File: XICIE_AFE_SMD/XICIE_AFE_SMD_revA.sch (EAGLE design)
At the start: 14 parts, among them IC1 LM324D, Q1 MOSFET-NCHANNELBSS123LT1G, Q2 MOSFET-NCHANNELBSS123LT1G

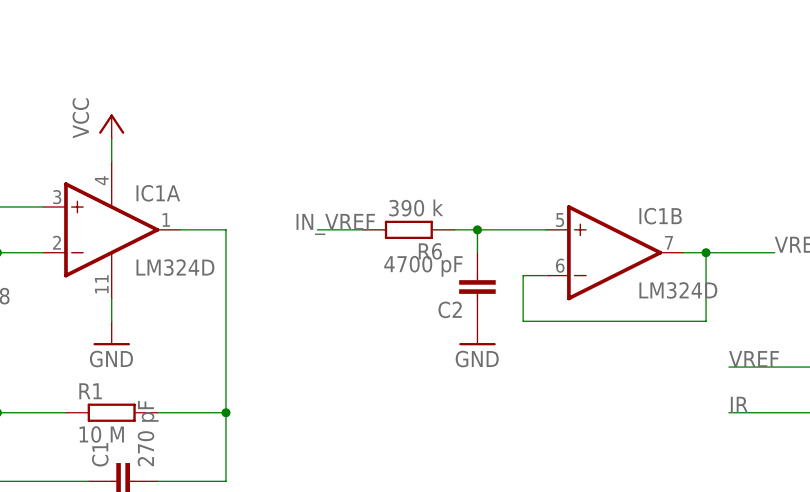
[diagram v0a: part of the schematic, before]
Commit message: Minor changes in afe_smd
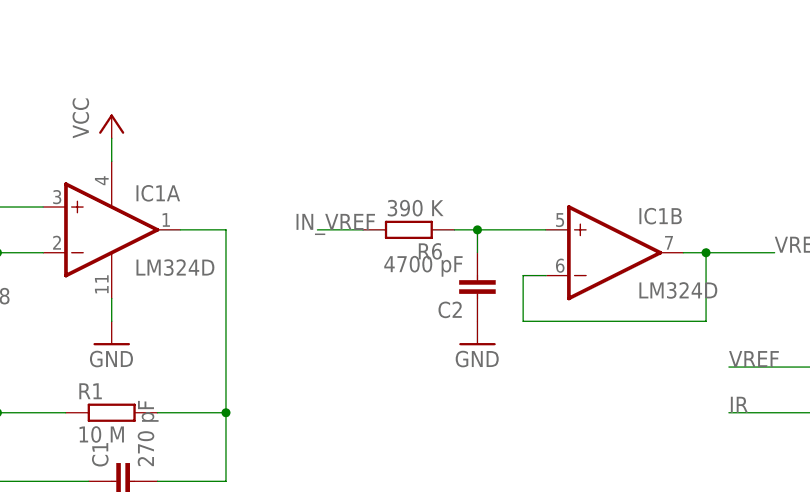
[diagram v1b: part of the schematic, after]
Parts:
- R6: value 390 k -> 390 K
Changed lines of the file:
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@@
 <part name="R4" library="rcl" deviceset="R-EU_" device="R0603" value="10"/>
 <part name="R5" library="rcl" deviceset="R-EU_" device="R0603" value="10"/>
-<part name="R6" library="rcl" deviceset="R-EU_" device="R0603" value="390 k"/>
+<part name="R6" library="rcl" deviceset="R-EU_" device="R0603" value="390 K"/>
 <part name="C2" library="rcl" deviceset="C-EU" device="C0402" value="4700 pF"/>
 <part name="GND4" library="supply1" deviceset="GND" device=""/>

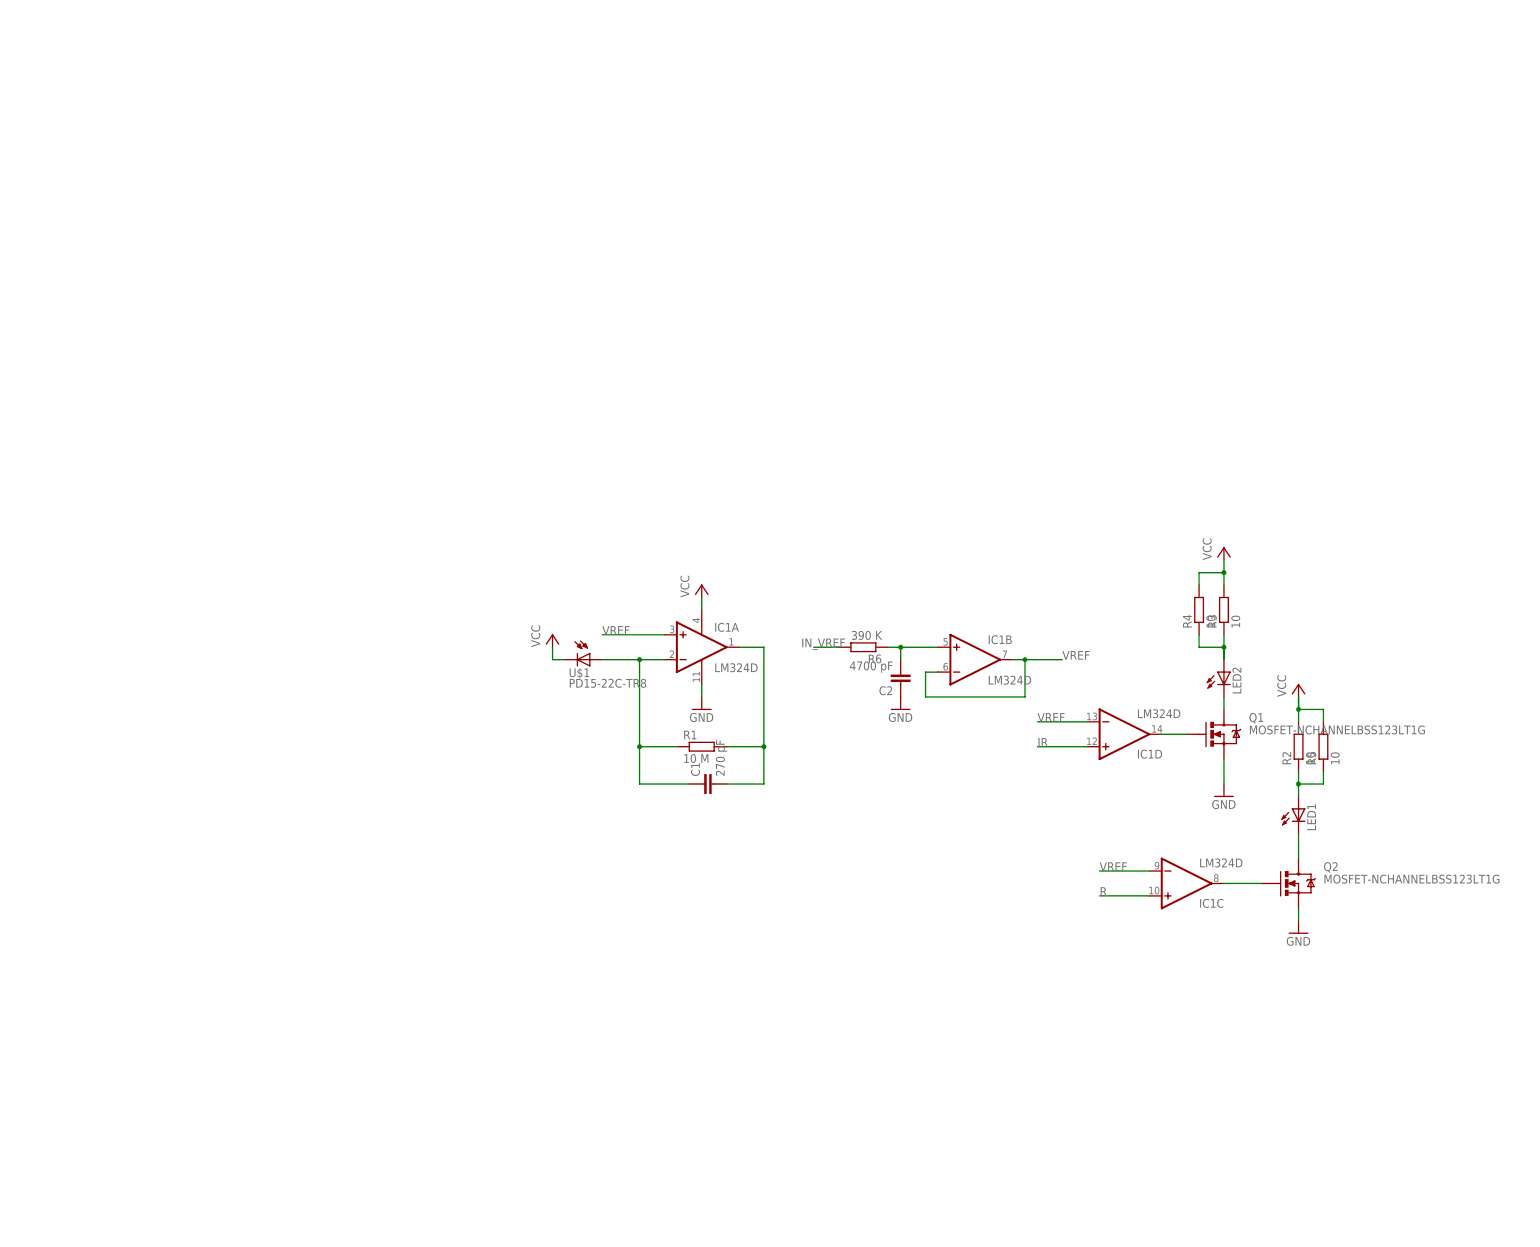
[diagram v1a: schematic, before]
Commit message: Added PSoc IC and boost converter
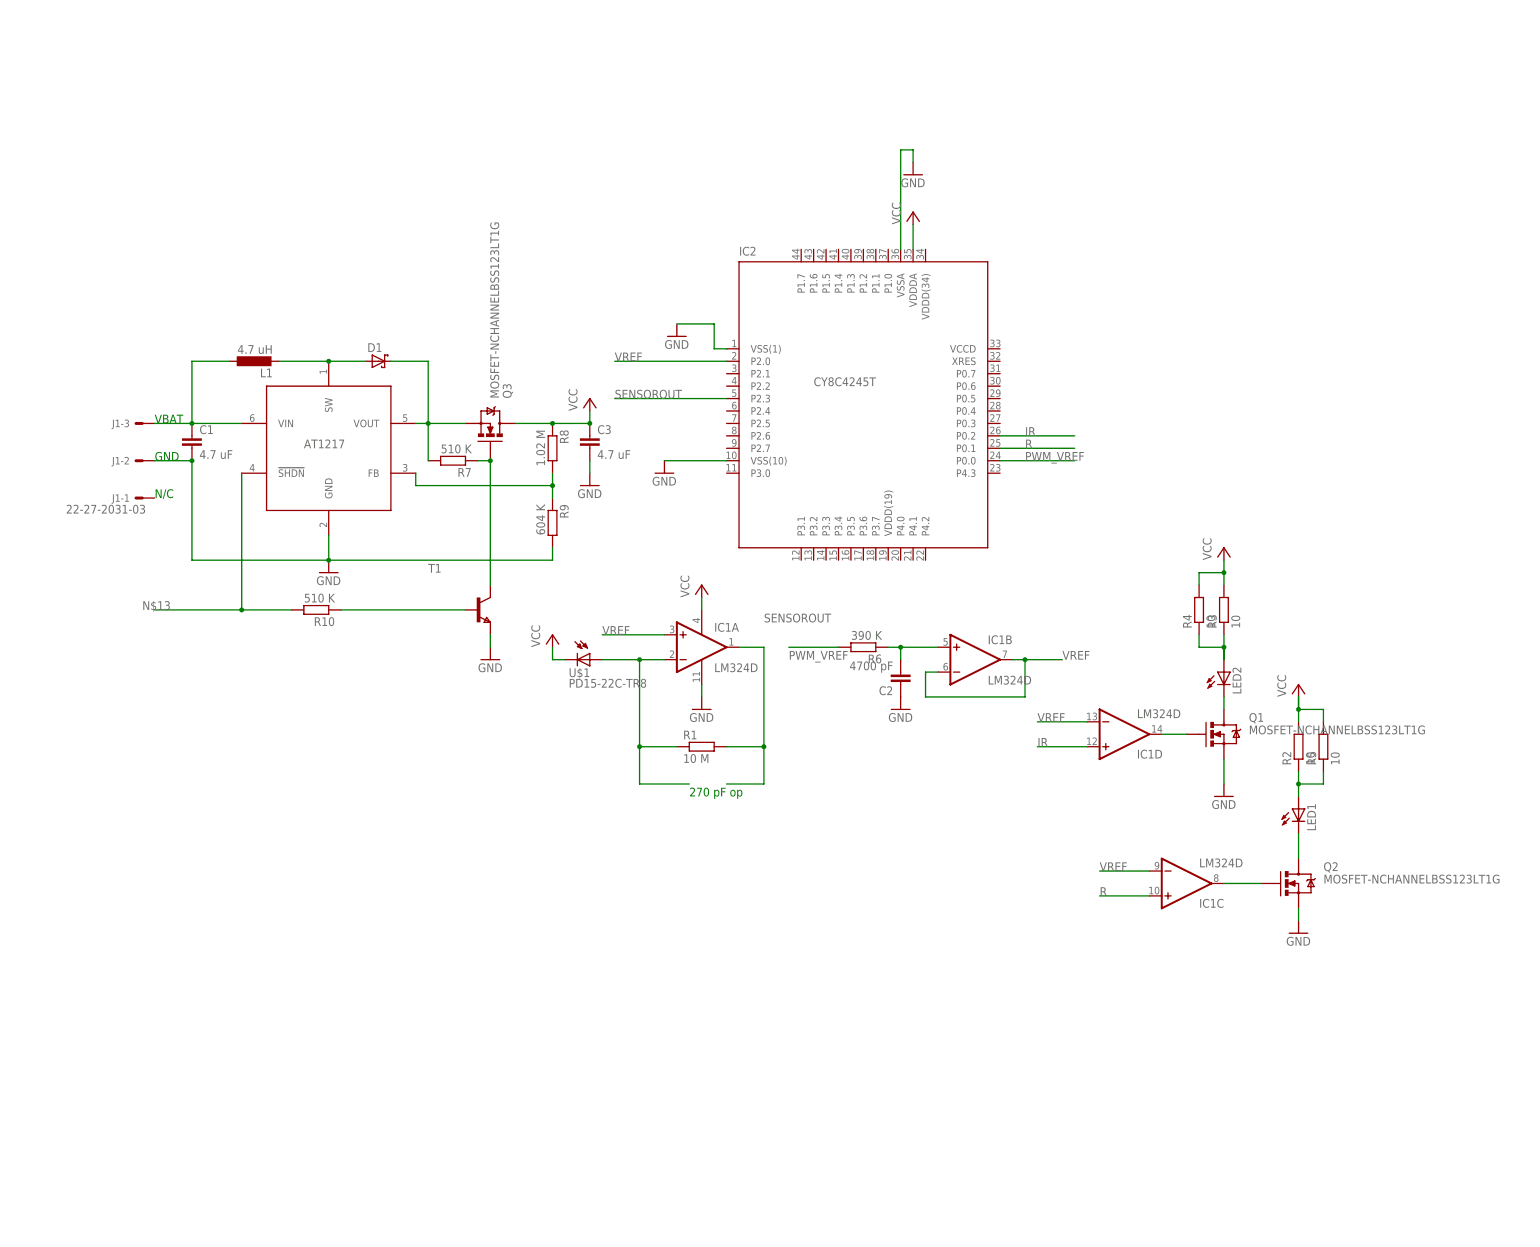
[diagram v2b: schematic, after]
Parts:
- added C3: 4.7 uF, rcl:C-EUC0603
- added D1: (no value), juliano:SCHOTTKY-DIODESMD
- added IC2: CY8C4245T, juliano:CY8C4245T
- added IC3: AAT1217, juliano:AAT1217
- added J1: 22-27-2031-03, con-molex:22-27-2031-03
- added L1: 4.7 uH, juliano:L-EU
- added Q3: MOSFET-NCHANNELBSS123LT1G, SparkFun-DiscreteSemi:MOSFET-NCHANNELBSS123LT1G
- added R10, R7: 510 K, rcl:R-EU_R0603
- added R8: 1.02 M, rcl:R-EU_R0805
- added R9: 604 K, rcl:R-EU_R0603
- added T1: (no value), zetex:NPNSOT23
- C1: value 270 pF -> 4.7 uF; device rcl:C-EUC0402 -> rcl:C-EUC0603
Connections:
- removed net IN_VREF: R6.2
- removed net TRANSOUT: C1.2, IC1A.OUT, R1.2
- new net N$10: C1.1, IC3.VIN, J1-3.S, L1.1
- new net N$11: D1.C, IC3.VOUT, Q3.S, R7.2
- new net N$12: Q3.G, R7.1, T1.C
- new net N$13: IC3.!SHDN, R10.2
- new net N$14: IC3.FB, R8.2, R9.1
- new net N$15: R10.1, T1.B
- new net N$2: D1.A, IC3.SW, L1.2
- new net PWM_VREF: IC2.P0.0, R6.2
- new net SENSOROUT: IC1A.OUT, IC2.P2.3, R1.2
- net GND: now also C1.2, C3.2, IC2.VSS(1), IC2.VSS(10), IC2.VSSA, IC3.GND, J1-2.S, R9.2, T1.E
- net IR: now also IC2.P0.2
- net N$1: no longer C1.1
- net R: now also IC2.P0.1
- net VCC: now also C3.1, IC2.VDDDA, Q3.D, R8.1
- net VREF: now also IC2.P2.0
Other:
- note added: "270 pF op"
- note added: "GND"
- note added: "N/C"
- note added: "VBAT"
- moved on the sheet: C1

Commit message: PCB Layoutd
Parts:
- removed Q3: MOSFET-NCHANNELBSS123LT1G, SparkFun-DiscreteSemi:MOSFET-NCHANNELBSS123LT1G
- removed R10, R7: 510 K, rcl:R-EU_R0603
- removed R5: 10, rcl:R-EU_R0603
- removed T1: (no value), zetex:NPNSOT23
- R2, R3: value 10 -> 1.1; device rcl:R-EU_R0603 -> rcl:R-EU_R0402
- R4: value 10 -> 1.02 M; device rcl:R-EU_R0603 -> rcl:R-EU_R0805
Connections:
- net N$2 renamed SW
- removed net N$10: C1.1, IC3.VIN, J1-3.S, L1.1
- removed net N$11: D1.C, IC3.VOUT, Q3.S, R7.2
- removed net N$12: Q3.G, R7.1, T1.C
- removed net N$13: IC3.!SHDN, R10.2
- removed net N$15: R10.1, T1.B
- new net SHUTDOWN: IC3.!SHDN, R4.2
- new net VBAT: C1.1, IC3.VIN, J1-3.S, L1.1, R4.1
- net GND: no longer T1.E
- net N$7: no longer R5.1
- net N$8: no longer R4.1
- net VCC: now also D1.C, IC3.VOUT; no longer Q3.D, R4.2, R5.2
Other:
- moved on the sheet: R4

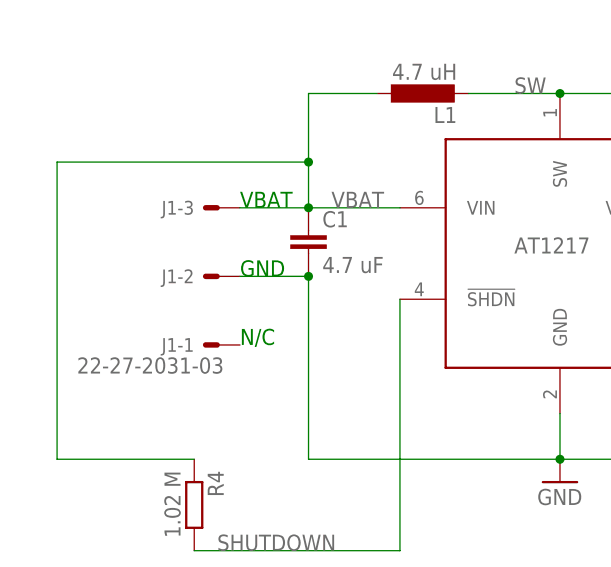
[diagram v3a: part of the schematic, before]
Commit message: Reduced outline
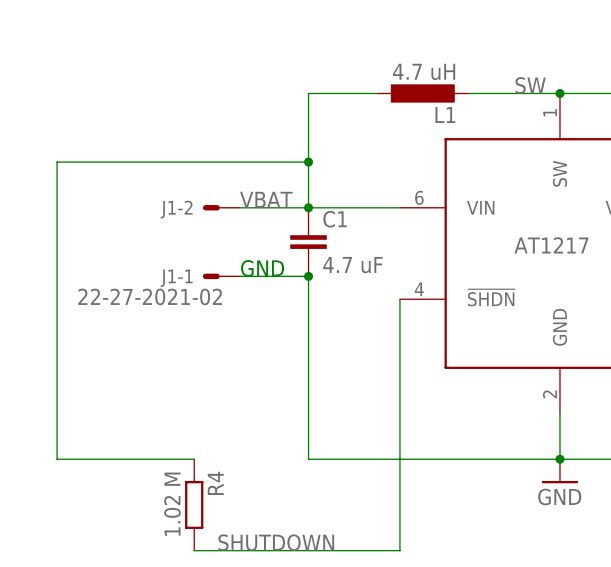
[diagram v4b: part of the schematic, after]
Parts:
- J1: value 22-27-2031-03 -> 22-27-2021-02; device con-molex:22-27-2031-03 -> con-molex:22-27-2021-02
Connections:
- net GND: now also J1-1.S; no longer J1-2.S
- net VBAT: now also J1-2.S; no longer J1-3.S
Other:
- note removed: "N/C"
- note removed: "VBAT"
- moved on the sheet: J1-1, J1-2
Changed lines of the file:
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@@
 <?xml version="1.0" encoding="utf-8"?>
 <!DOCTYPE eagle SYSTEM "eagle.dtd">
-<eagle version="6.4">
+<eagle version="6.5.0">
 <drawing>
 <settings>
@@
 <grid distance="0.1" unitdist="inch" unit="inch" style="lines" multiple="1" display="yes" altdistance="0.01" altunitdist="inch" altunit="inch"/>
 <layers>
-<layer number="1" name="Top" color="4" fill="1" visible="no" active="no"/>
-<layer number="16" name="Bottom" color="1" fill="1" visible="no" active="no"/>
-<layer number="17" name="Pads" color="2" fill="1" visible="no" active="no"/>
-<layer number="18" name="Vias" color="2" fill="1" visible="no" active="no"/>
-<layer number="19" name="Unrouted" color="6" fill="1" visible="no" active="no"/>
-<layer number="20" name="Dimension" color="15" fill="1" visible="no" active="no"/>
-<layer number="21" name="tPlace" color="7" fill="1" visible="no" active="no"/>
-<layer number="22" name="bPlace" color="7" fill="1" visible="no" active="no"/>
-<layer number="23" name="tOrigins" color="15" fill="1" visible="no" active="no"/>
-<layer number="24" name="bOrigins" color="15" fill="1" visible="no" active="no"/>
-<layer number="25" name="tNames" color="7" fill="1" visible="no" active="no"/>
-<layer number="26" name="bNames" color="7" fill="1" visible="no" active="no"/>
-<layer number="27" name="tValues" color="7" fill="1" visible="no" active="no"/>
-<layer number="28" name="bValues" color="7" fill="1" visible="no" active="no"/>
+<layer number="1" name="Top" color="4" fill="1" visible="yes" active="no"/>
+<layer number="16" name="Bottom" color="1" fill="1" visible="yes" active="no"/>
+<layer number="17" name="Pads" color="2" fill="1" visible="yes" active="no"/>
+<layer number="18" name="Vias" color="2" fill="1" visible="yes" active="no"/>
+<layer number="19" name="Unrouted" color="6" fill="1" visible="yes" active="no"/>
+<layer number="20" name="Dimension" color="15" fill="1" visible="yes" active="no"/>
+<layer number="21" name="tPlace" color="7" fill="1" visible="yes" active="no"/>
+<layer number="22" name="bPlace" color="7" fill="1" visible="yes" active="no"/>
+<layer number="23" name="tOrigins" color="15" fill="1" visible="yes" active="no"/>
+<layer number="24" name="bOrigins" color="15" fill="1" visible="yes" active="no"/>
+<layer number="25" name="tNames" color="7" fill="1" visible="yes" active="no"/>
+<layer number="26" name="bNames" color="7" fill="1" visible="yes" active="no"/>
+<layer number="27" name="tValues" color="7" fill="1" visible="yes" active="no"/>
+<layer number="28" name="bValues" color="7" fill="1" visible="yes" active="no"/>
 <layer number="29" name="tStop" color="7" fill="3" visible="no" active="no"/>
 <layer number="30" name="bStop" color="7" fill="6" visible="no" active="no"/>
@@
 <layer number="35" name="tGlue" color="7" fill="4" visible="no" active="no"/>
 <layer number="36" name="bGlue" color="7" fill="5" visible="no" active="no"/>
-<layer number="37" name="tTest" color="7" fill="1" visible="no" active="no"/>
-<layer number="38" name="bTest" color="7" fill="1" visible="no" active="no"/>
+<layer number="37" name="tTest" color="7" fill="1" visible="yes" active="no"/>
+<layer number="38" name="bTest" color="7" fill="1" visible="yes" active="no"/>
 <layer number="39" name="tKeepout" color="4" fill="11" visible="no" active="no"/>
 <layer number="40" name="bKeepout" color="1" fill="11" visible="no" active="no"/>
@@
 <layer number="44" name="Drills" color="7" fill="1" visible="no" active="no"/>
 <layer number="45" name="Holes" color="7" fill="1" visible="no" active="no"/>
-<layer number="46" name="Milling" color="3" fill="1" visible="no" active="no"/>
-<layer number="47" name="Measures" color="7" fill="1" visible="no" active="no"/>
-<layer number="48" name="Document" color="7" fill="1" visible="no" active="no"/>
-<layer number="49" name="Reference" color="7" fill="1" visible="no" active="no"/>
-<layer number="50" name="dxf" color="7" fill="1" visible="no" active="no"/>
-<layer number="51" name="tDocu" color="7" fill="1" visible="no" active="no"/>
-<layer number="52" name="bDocu" color="7" fill="1" visible="no" active="no"/>
-<layer number="53" name="tGND_GNDA" color="7" fill="9" visible="no" active="no"/>
-<layer number="54" name="bGND_GNDA" color="1" fill="9" visible="no" active="no"/>
-<layer number="56" name="wert" color="7" fill="1" visible="no" active="no"/>
+<layer number="46" name="Milling" color="3" fill="1" visible="yes" active="no"/>
+<layer number="47" name="Measures" color="7" fill="1" visible="yes" active="no"/>
+<layer number="48" name="Document" color="7" fill="1" visible="yes" active="no"/>
+<layer number="49" name="Reference" color="7" fill="1" visible="yes" active="no"/>
+<layer number="50" name="dxf" color="7" fill="1" visible="yes" active="no"/>
+<layer number="51" name="tDocu" color="7" fill="1" visible="yes" active="no"/>
+<layer number="52" name="bDocu" color="7" fill="1" visible="yes" active="no"/>
+<layer number="53" name="tGND_GNDA" color="7" fill="9" visible="yes" active="no"/>
+<layer number="54" name="bGND_GNDA" color="1" fill="9" visible="yes" active="no"/>
+<layer number="56" name="wert" color="7" fill="1" visible="yes" active="no"/>
 <layer number="91" name="Nets" color="2" fill="1" visible="yes" active="yes"/>
 <layer number="92" name="Busses" color="1" fill="1" visible="yes" active="yes"/>
@@
 <class number="0" name="default" width="0" drill="0">
 </class>
-<class number="1" name="GND" width="0.254" drill="0">
-<clearance class="1" value="0.254"/>
+<class number="1" name="GND" width="0" drill="0">
 </class>
-<class number="2" name="V" width="0.254" drill="0">
-<clearance class="2" value="0.1016"/>
+<class number="2" name="V" width="0" drill="0">
 </class>
 </classes>
@@
 <part name="GND7" library="supply1" deviceset="GND" device=""/>
 <part name="IC3" library="juliano" deviceset="AAT1217" device=""/>
-<part name="J1" library="con-molex" deviceset="22-?-03" device="27-2031"/>
 <part name="GND8" library="supply1" deviceset="GND" device=""/>
 <part name="C1" library="rcl" deviceset="C-EU" device="C0603" value="4.7 uF"/>
@@
 <part name="D1" library="juliano" deviceset="SCHOTTKY-DIODE" device="SMD"/>
 <part name="R4" library="rcl" deviceset="R-EU_" device="R0805" value="1.02 M"/>
+<part name="J1" library="con-molex" deviceset="22-?-02" device="27-2021"/>
 </parts>
 <sheets>
@@
 <text x="30.48" y="58.42" size="1.778" layer="91">270 pF op</text>
 <text x="-78.74" y="127" size="1.778" layer="91">GND</text>
-<text x="-78.74" y="134.62" size="1.778" layer="91">VBAT</text>
-<text x="-78.74" y="119.38" size="1.778" layer="91">N/C</text>
 </plain>
 <instances>
@@
 <instance part="GND7" gate="1" x="76.2" y="185.42"/>
 <instance part="IC3" gate="G$1" x="-43.18" y="129.54"/>
-<instance part="J1" gate="-1" x="-81.28" y="119.38" rot="R180"/>
-<instance part="J1" gate="-2" x="-81.28" y="127" rot="R180"/>
-<instance part="J1" gate="-3" x="-81.28" y="134.62" rot="R180"/>
 <instance part="GND8" gate="1" x="-43.18" y="104.14"/>
 <instance part="C1" gate="G$1" x="-71.12" y="132.08"/>
@@
 <instance part="D1" gate="G$1" x="-33.02" y="147.32"/>
 <instance part="R4" gate="G$1" x="-83.82" y="101.6" rot="R270"/>
+<instance part="J1" gate="-1" x="-81.28" y="127" rot="R180"/>
+<instance part="J1" gate="-2" x="-81.28" y="134.62" rot="R180"/>
 </instances>
 <busses>
@@
 </segment>
 <segment>
-<pinref part="J1" gate="-2" pin="S"/>
-<wire x1="-78.74" y1="127" x2="-71.12" y2="127" width="0.1524" layer="91"/>
 <wire x1="-71.12" y1="127" x2="-71.12" y2="106.68" width="0.1524" layer="91"/>
 <wire x1="-71.12" y1="106.68" x2="-43.18" y2="106.68" width="0.1524" layer="91"/>
@@
 <junction x="-43.18" y="106.68"/>
 <pinref part="C1" gate="G$1" pin="2"/>
-<junction x="-71.12" y="127"/>
 <pinref part="R9" gate="G$1" pin="2"/>
 <wire x1="2.54" y1="109.22" x2="2.54" y2="106.68" width="0.1524" layer="91"/>
 <wire x1="2.54" y1="106.68" x2="-43.18" y2="106.68" width="0.1524" layer="91"/>
+<pinref part="J1" gate="-1" pin="S"/>
+<wire x1="-78.74" y1="127" x2="-71.12" y2="127" width="0.1524" layer="91"/>
+<junction x="-71.12" y="127"/>
 </segment>
 <segment>
@@
 <net name="VBAT" class="2">
 <segment>
-<pinref part="J1" gate="-3" pin="S"/>
-<wire x1="-78.74" y1="134.62" x2="-71.12" y2="134.62" width="0.1524" layer="91"/>
 <pinref part="IC3" gate="G$1" pin="VIN"/>
 <wire x1="-71.12" y1="134.62" x2="-60.96" y2="134.62" width="0.1524" layer="91"/>
@@
 <wire x1="-99.06" y1="139.7" x2="-71.12" y2="139.7" width="0.1524" layer="91"/>
 <junction x="-71.12" y="139.7"/>
-<label x="-68.58" y="134.62" size="1.778" layer="95"/>
-</segment>
-</net>
+<label x="-78.74" y="134.62" size="1.778" layer="95"/>
+<pinref part="J1" gate="-2" pin="S"/>
+<wire x1="-78.74" y1="134.62" x2="-71.12" y2="134.62" width="0.1524" layer="91"/>
+</segment>
+</net>
